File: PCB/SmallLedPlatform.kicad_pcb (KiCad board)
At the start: 4 copper layers, 63.5 x 36.1 mm, 110 parts, among them J101 Conn_01x03_Male, J102 USB_C_Receptacle, J103 Conn_01x03_Male, J104 Conn_02x05_Odd_Even, Q101 AO3400A, Q201 IRFR7440TRPBF, Q202 IRFR7440TRPBF, Q301 2N7002, Q302 2N7002, Q303 2N7002, Q304 2N7002, SW401 SW_MEC_5E, SW402 SW_MEC_5E, U101 STM32G0B1CBTx, U102 USBLC6-2P6, U103 TCPP01-M12, U201 LM25118, U202 XC6206PxxxMR, U203 WS3222D, U204 WS3222D, U401 AP3722AT

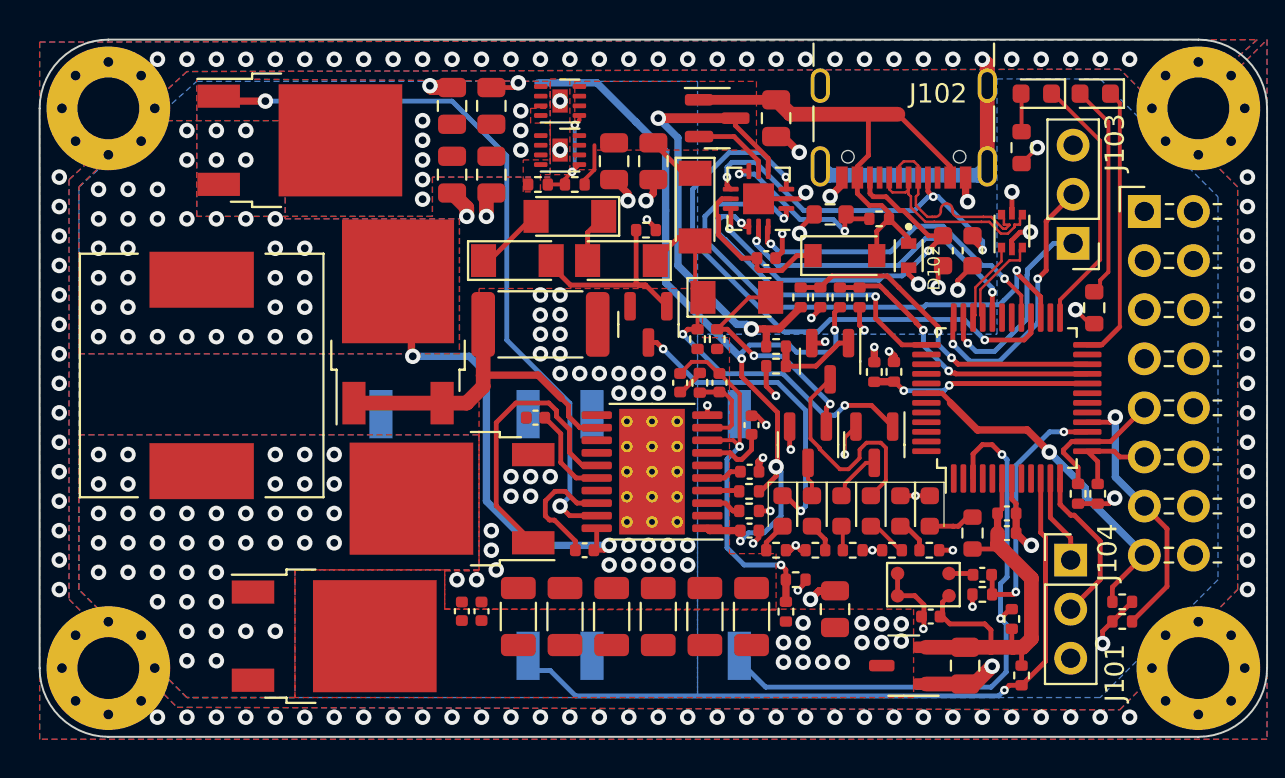
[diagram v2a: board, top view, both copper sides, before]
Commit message: Add LEDs for each USBPD level and a microphone
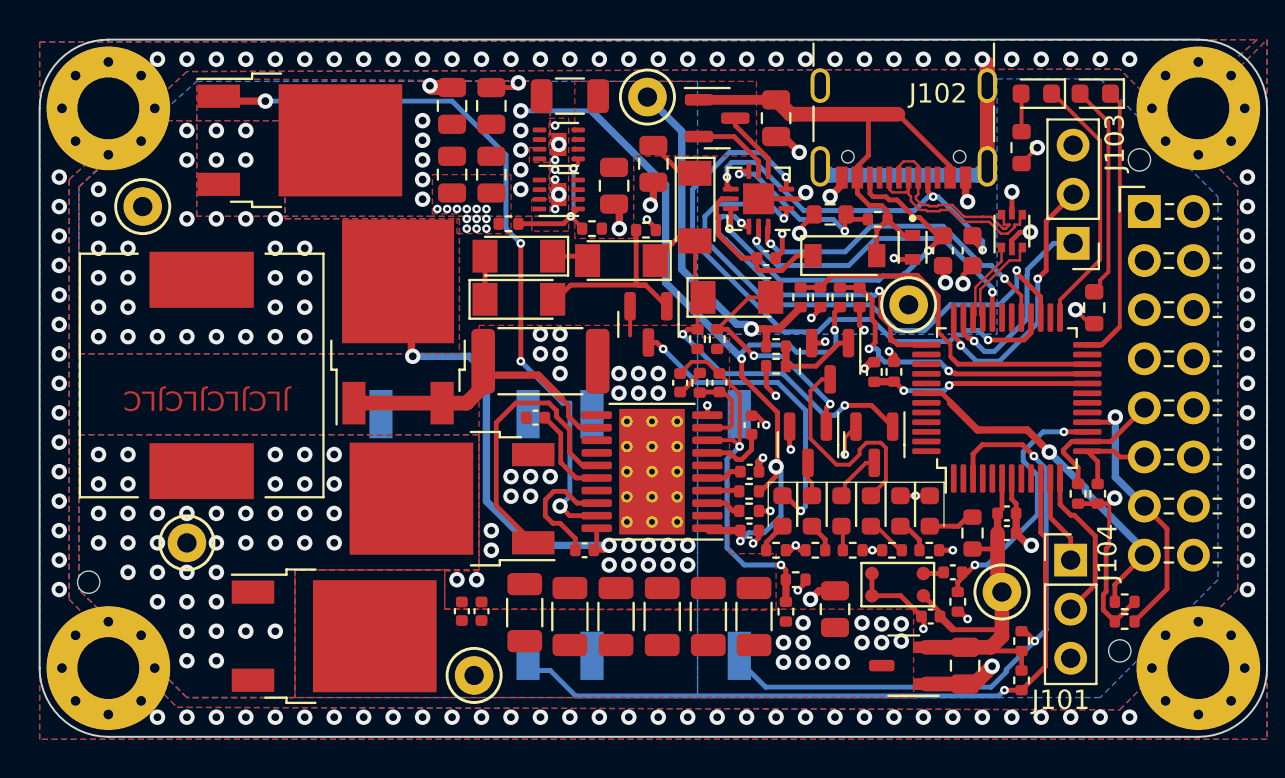
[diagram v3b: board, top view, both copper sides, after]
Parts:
- added H105: ToolingHole, JLC:JLC_toolinghole, F.Cu at (94.0, 106.8)
- added H106: ToolingHole, JLC:JLC_toolinghole, F.Cu at (148.3, 85.0)
- added H107: ToolingHole, JLC:JLC_toolinghole, F.Cu at (147.3, 110.4)
- added R211: 100R, Resistor_SMD:R_1206_3216Metric, F.Cu at (118.9, 81.7)
- added TP101: TestPoint, TestPoint:TestPoint_Keystone_5000-5004_Miniature, F.Cu at (113.9, 111.6)
- added TP102: TestPoint, TestPoint:TestPoint_Keystone_5000-5004_Miniature, F.Cu at (136.4, 92.5)
- added TP103: TestPoint, TestPoint:TestPoint_Keystone_5000-5004_Miniature, F.Cu at (122.9, 81.7)
- added TP201: TestPoint, TestPoint:TestPoint_Keystone_5000-5004_Miniature, F.Cu at (141.2, 107.3)
- added TP202: TestPoint, TestPoint:TestPoint_Keystone_5000-5004_Miniature, F.Cu at (96.8, 87.4)
- added TP203: TestPoint, TestPoint:TestPoint_Keystone_5000-5004_Miniature, F.Cu at (99.1, 104.8)
- C218: renamed from C220; value 470nF/6.3V -> 470nF/10V
- moved D310 3.35 mm to (116.2, 89.9)
- moved R213 2.54 mm to (115.7, 88.3)
- moved R212 2.45 mm to (120.0, 88.5)
- moved U204 2.30 mm to (118.3, 86.8)
- moved U203 2.25 mm to (118.3, 84.2)
- moved D311 2.01 mm to (116.2, 92.2)
- moved R202 1.91 mm to (117.3, 95.4)
- moved C402 1.53 mm to (138.7, 106.3)
- moved R401 1.33 mm to (138.9, 107.8), turned to -90 degrees
- moved U401 1.32 mm to (137.2, 107.5)
- moved C221 1.27 mm to (121.2, 86.3)
- moved R403 1.25 mm to (142.2, 109.9)
- moved D102 0.48 mm to (136.6, 89.5)
- moved C213 0.39 mm to (116.5, 108.4)
- moved C214 0.25 mm to (118.9, 108.6)
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- renumbered C219 to C217, C221 to C219, C222 to C220, C217 to C221, C218 to C222, R211 to R212, R212 to R213
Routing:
- net +5V: track 12.5 -> 17.9 mm, vias 23 -> 22
- net IN: track 29.6 -> 24.6 mm, vias 2 -> 1
- net /MCU_SW2: track 30.3 -> 32.7 mm
- net /Power/OVLO: track 5.30 -> 7.36 mm
- net /Power/CS: track 17.6 -> 15.7 mm
- net GND: track 50.8 -> 49.2 mm, vias 73 -> 81
- net Net-(D310-Pad2): track 3.66 -> 2.24 mm
- net +3V3: track 23.0 -> 21.6 mm
- net /Power/VIN_SENSE: track 15.2 -> 16.6 mm
- net /CC2_MCU: track 28.5 -> 29.5 mm
- net /VBUS_SENSE: track 17.5 -> 18.5 mm, vias 2 -> 0
- net /USB_DATA_N: track 11.0 -> 10.0 mm
- net Net-(D303-Pad2): track 2.63 -> 1.90 mm
- net /Power/VIN: track 43.8 -> 43.1 mm, vias 12 -> 14
- net /~{DB}_MCU: track 16.4 -> 17.1 mm
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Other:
- board text added: "JLCJLCJLCJLC"

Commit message: Prepare board for manufactoring
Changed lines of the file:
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@@
     )
     (pad_to_mask_clearance 0)
-    (aux_axis_origin 91.44 78.867)
-    (grid_origin 91.44 78.867)
+    (aux_axis_origin 91.44 78.74)
+    (grid_origin 91.44 78.74)
     (pcbplotparams
       (layerselection 0x00010fc_ffffffff)
@@
     (property "Sheetname" "")
     (attr through_hole)
-    (fp_text reference "J101" (at -0.508 7.239 180) (layer "F.SilkS")
-      (effects (font (size 1 1) (thickness 0.15)))
+    (fp_text reference "J101" (at -1.016 -3.275359 -270) (layer "B.SilkS")
+      (effects (font (size 1 1) (thickness 0.15)) (justify mirror))
     )
     (fp_text value "Conn_01x03_Male" (at 0 7.41) (layer "F.Fab")
@@
     (property "Sheetname" "")
     (attr smd)
-    (fp_text reference "J102" (at -1.778 0.6604 unlocked) (layer "F.SilkS")
-      (effects (font (size 1 1) (thickness 0.15)))
+    (fp_text reference "J102" (at -1.778 0.6604 unlocked) (layer "B.SilkS")
+      (effects (font (size 1 1) (thickness 0.15)) (justify mirror))
     )
     (fp_text value "USB_C_Receptacle" (at 0 5 180 unlocked) (layer "F.Fab")
@@
     (property "Sheetname" "")
     (attr through_hole)
-    (fp_text reference "J104" (at -1.905 17.653 90) (layer "F.SilkS")
-      (effects (font (size 1 1) (thickness 0.15)))
+    (fp_text reference "J104" (at -1.905 7.874 -90) (layer "B.SilkS")
+      (effects (font (size 1 1) (thickness 0.15)) (justify mirror))
     )
     (fp_text value "Conn_02x05_Odd_Even" (at 5.655 20.05) (layer "F.Fab")
@@
     (property "Sheetname" "")
     (attr through_hole)
-    (fp_text reference "J103" (at -2.159 5.207 90) (layer "F.SilkS")
-      (effects (font (size 1 1) (thickness 0.15)))
+    (fp_text reference "J103" (at 2.267054 -0.165 270) (layer "B.SilkS")
+      (effects (font (size 1 1) (thickness 0.15)) (justify mirror))
     )
     (fp_text value "Conn_01x03_Male" (at 0 7.41) (layer "F.Fab")
@@
         (xy 154.94 114.935)
         (xy 91.44 114.935)
-        (xy 91.44 78.867)
+        (xy 91.44 78.74)
         (xy 154.432 78.74)
         (xy 149.86 82.804)
@@
       )
     )
+  )
+  (zone (net 0) (net_name "") (layers *.Mask) (hatch edge 0.508)
+    (connect_pads (clearance 0.254))
+    (min_thickness 0.254) (filled_areas_thickness no)
+    (fill yes (thermal_gap 0.508) (thermal_bridge_width 0.508))
+    (polygon
+      (pts
+        (xy 154.94 84.836)
+        (xy 149.352 84.963)
+        (xy 149.352 78.74)
+        (xy 154.94 78.74)
+      )
+    )
+  )
+  (zone (net 0) (net_name "") (layers *.Mask) (hatch edge 0.508)
+    (connect_pads (clearance 0.254))
+    (min_thickness 0.254) (filled_areas_thickness no)
+    (fill yes (thermal_gap 0.508) (thermal_bridge_width 0.508))
+    (polygon
+      (pts
+        (xy 155.448 115.951)
+        (xy 90.932 115.950986)
+        (xy 90.933016 78.231988)
+        (xy 154.941016 78.359002)
+        (xy 149.987 82.931)
+        (xy 147.2692 80.264)
+        (xy 99.06 80.391)
+        (xy 92.964 85.979)
+        (xy 92.964 107.696)
+        (xy 98.552 113.284)
+        (xy 147.3454 113.411)
+        (xy 153.416 107.188)
+        (xy 153.416 86.36)
+        (xy 150.495 83.439)
+        (xy 155.448 78.74)
+      )
+    )

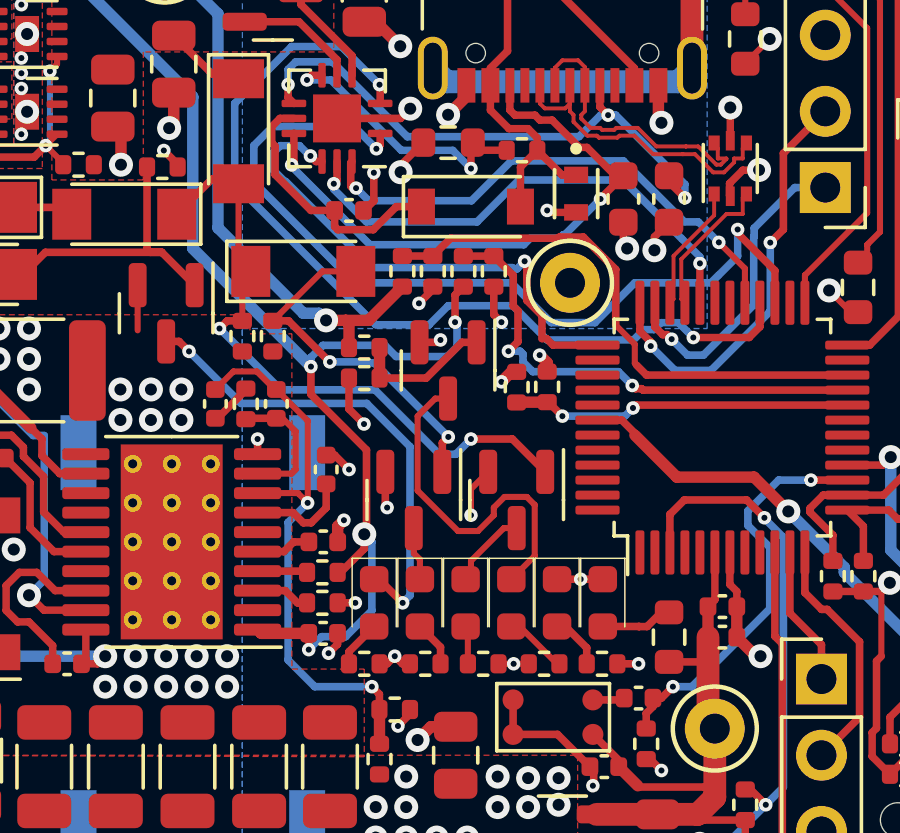
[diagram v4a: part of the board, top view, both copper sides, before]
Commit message: Add fan header on backside of board
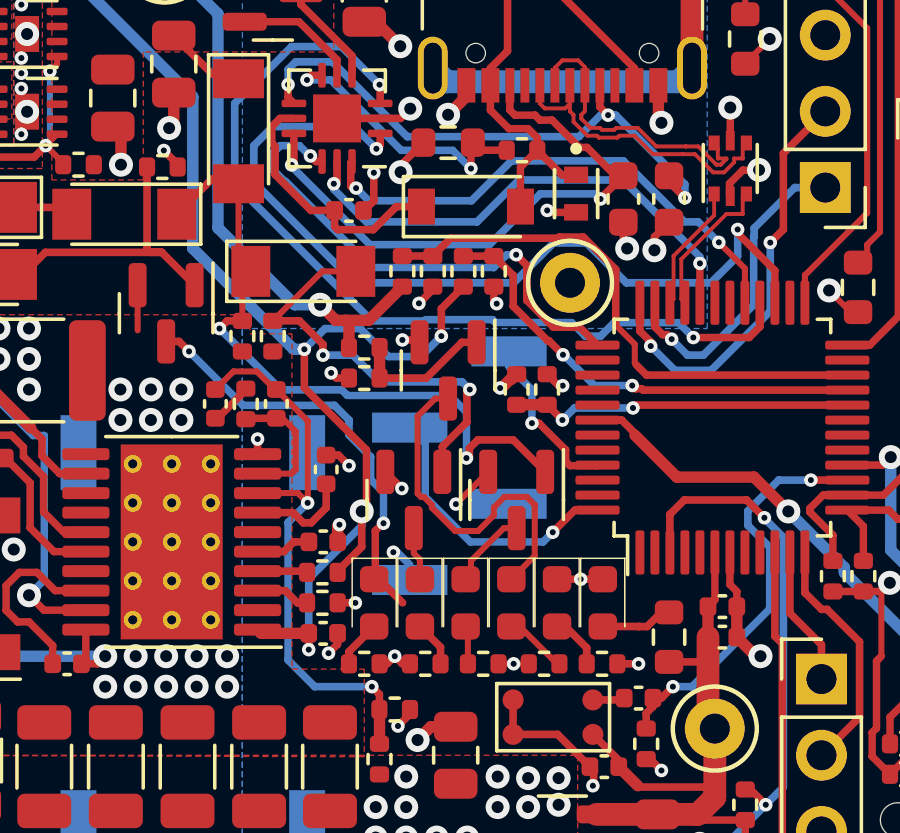
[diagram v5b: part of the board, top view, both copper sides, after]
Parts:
- added M101: Fan_4pin, Connector_PinHeader_2.54mm:PinHeader_1x04_P2.54mm_Vertical_SMD_Pin1Left, B.Cu at (132.7, 98.6)
- moved R209 0.09 mm to (135.6, 96.0)
- moved R206 0.08 mm to (134.6, 96.0)
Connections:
- U101 pad 45: unconnected-(U101-Pad45) -> Net-(U101-Pad45)
- U101 pad 48: unconnected-(U101-Pad48) -> Net-(U101-Pad48)
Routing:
- net Net-(U101-Pad48): track 0.00 -> 9.45 mm, vias 0 -> 1
- net Net-(U101-Pad45): track 0.00 -> 5.71 mm, vias 0 -> 1
- net /Power/Power LEDS/15v_gate: track 12.2 -> 14.3 mm
- net GND: track 49.2 -> 47.2 mm, vias 81 -> 82
- net /Power/Power LEDS/20v_led_k: track 16.2 -> 14.4 mm
- net /Power/VIN_SENSE: track 16.6 -> 15.2 mm
- net /Power/Power LEDS/9v_gate: track 21.5 -> 22.7 mm
- net /CC1_MCU: track 30.8 -> 30.2 mm
